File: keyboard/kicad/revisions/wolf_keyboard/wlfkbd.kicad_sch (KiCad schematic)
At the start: 0 parts

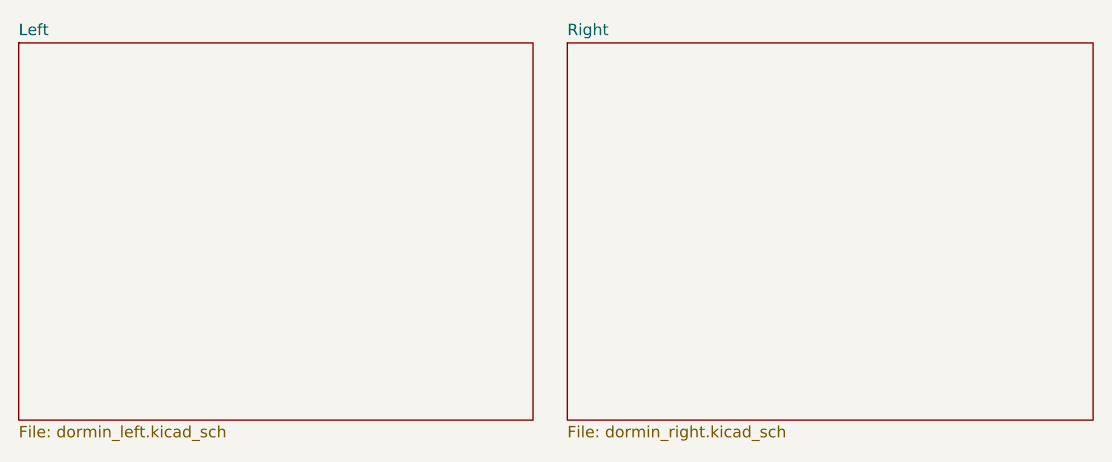
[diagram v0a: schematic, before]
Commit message: feat: fix schematics after renaming files
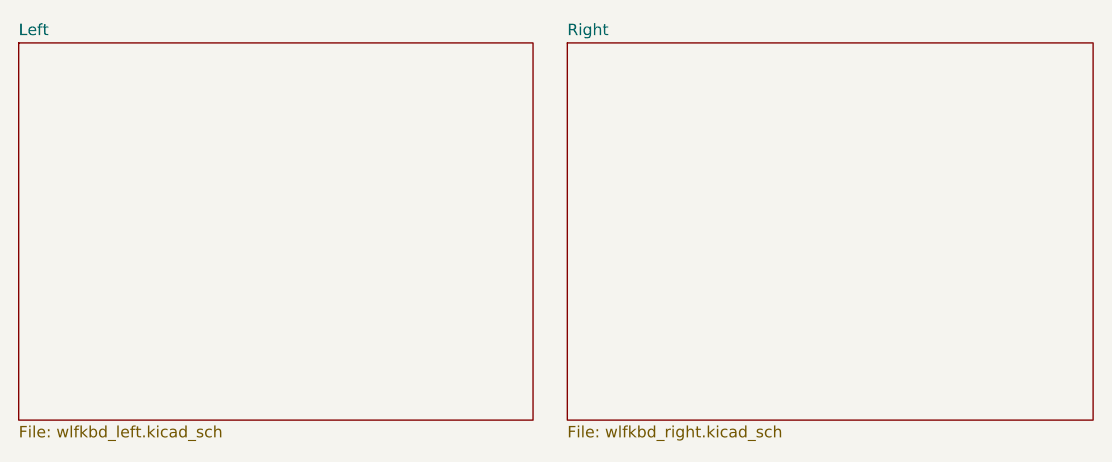
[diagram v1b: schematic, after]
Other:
- sheet Left: file dormin_left.kicad_sch -> wlfkbd_left.kicad_sch
- sheet Right: file dormin_right.kicad_sch -> wlfkbd_right.kicad_sch
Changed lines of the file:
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@@
 			)
 		)
-		(property "Sheetfile" "dormin_left.kicad_sch"
+		(property "Sheetfile" "wlfkbd_left.kicad_sch"
 			(at 44.45 84.4046 0)
 			(show_name no)
@@
 		)
 		(instances
-			(project "dormin"
+			(project "wlfkbd"
 				(path "/603afaa0-4142-4673-b835-76ba767ab9eb"
 					(page "2")
@@
 			)
 		)
-		(property "Sheetfile" "dormin_right.kicad_sch"
+		(property "Sheetfile" "wlfkbd_right.kicad_sch"
 			(at 105.41 84.4046 0)
 			(show_name no)
@@
 		)
 		(instances
-			(project "dormin"
+			(project "wlfkbd"
 				(path "/603afaa0-4142-4673-b835-76ba767ab9eb"
 					(page "3")

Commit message: chore: fix traces and orgaize schematics
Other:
- title: Dormin Keyboard -> Wolf Keyboard
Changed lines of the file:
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@@
 	(paper "A5")
 	(title_block
-		(title "Dormin Keyboard")
-		(date "2026-07-19")
+		(title "Wolf Keyboard")
+		(date "2026-09-07")
 		(rev "1.0.0")
-		(comment 1 "Left Half")
+		(comment 1 "The WLF is a 40-key split keyboard (20 keys per half).")
 		(comment 2 "Author: William A. Costa")
 	)
